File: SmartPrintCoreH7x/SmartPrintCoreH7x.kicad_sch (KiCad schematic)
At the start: 36 parts, among them SW1 BOOT, SW2 RST, U1 STM32H743ZITx, Y1 NX2016SA-25MHZ-EXS00A-CS11321

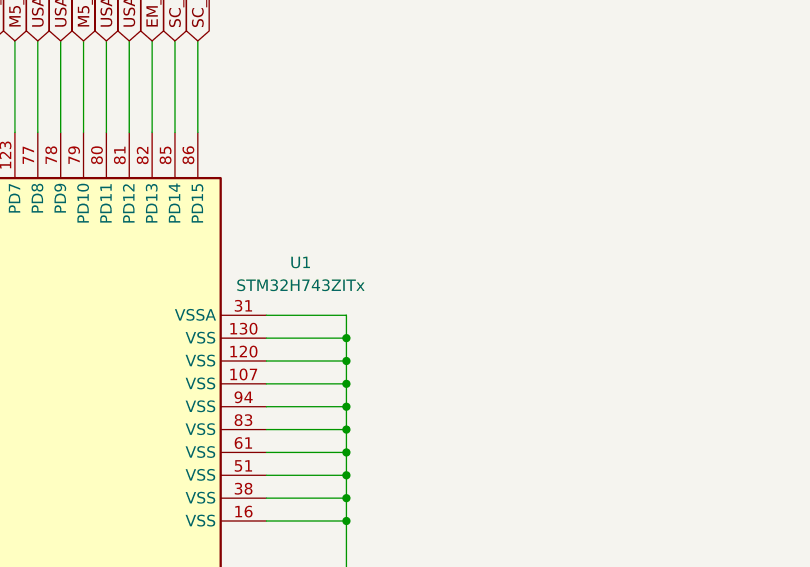
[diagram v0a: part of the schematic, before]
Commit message: MCU MPN Corrections and Readme update
Corrected MCU MPN to STM32H723ZGT6 (Note - user can choose from any variant compatible with STM32H723ZGT6 footprint and pin layout)
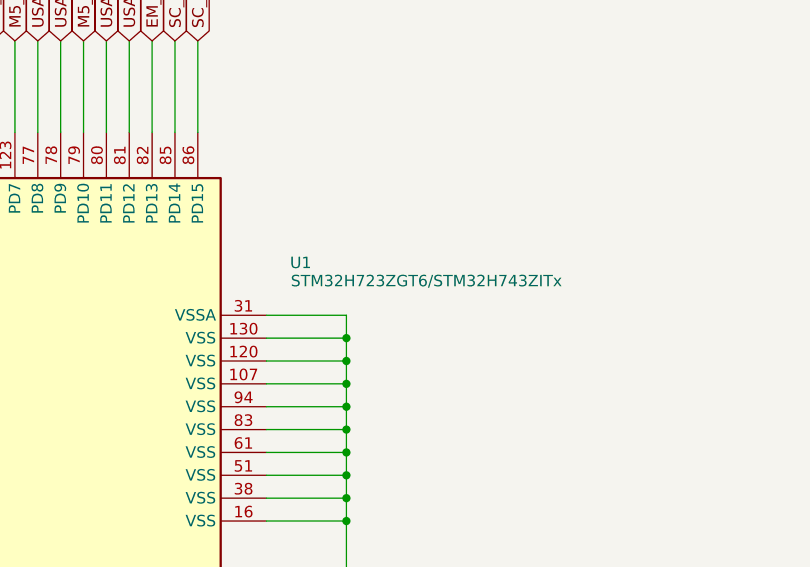
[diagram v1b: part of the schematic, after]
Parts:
- U1: value STM32H743ZITx -> STM32H723ZGT6/STM32H743ZITx; Manufacturer_Part_Number STM32H743ZIT6 -> STM32H723ZGT6
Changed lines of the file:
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@@
   )
   (symbol (lib_id "MCU_ST_STM32H7:STM32H743ZITx") (at 275.59 173.99 90) (unit 1)
-    (in_bom yes) (on_board yes) (dnp no) (fields_autoplaced)
+    (in_bom yes) (on_board yes) (dnp no)
     (property "Reference" "U1" (at 370.84 158.0005 90)
       (effects (font (size 1.27 1.27)))
     )
-    (property "Value" "STM32H743ZITx" (at 370.84 160.5405 90)
+    (property "Value" "STM32H723ZGT6/STM32H743ZITx" (at 384.81 160.02 90)
       (effects (font (size 1.27 1.27)))
     )
@@
       (effects (font (size 1.27 1.27)) hide)
     )
-    (property "Manufacturer_Part_Number" "STM32H743ZIT6" (at 275.59 173.99 0)
+    (property "Manufacturer_Part_Number" "STM32H723ZGT6" (at 275.59 173.99 0)
       (effects (font (size 1.27 1.27)) hide)
     )
